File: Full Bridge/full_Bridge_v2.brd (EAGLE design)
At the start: 118.4 x 84.4 mm, 28 parts, among them Q1 IRF520, Q4 IRF520, Q5 IRF520, Q8 IRF520

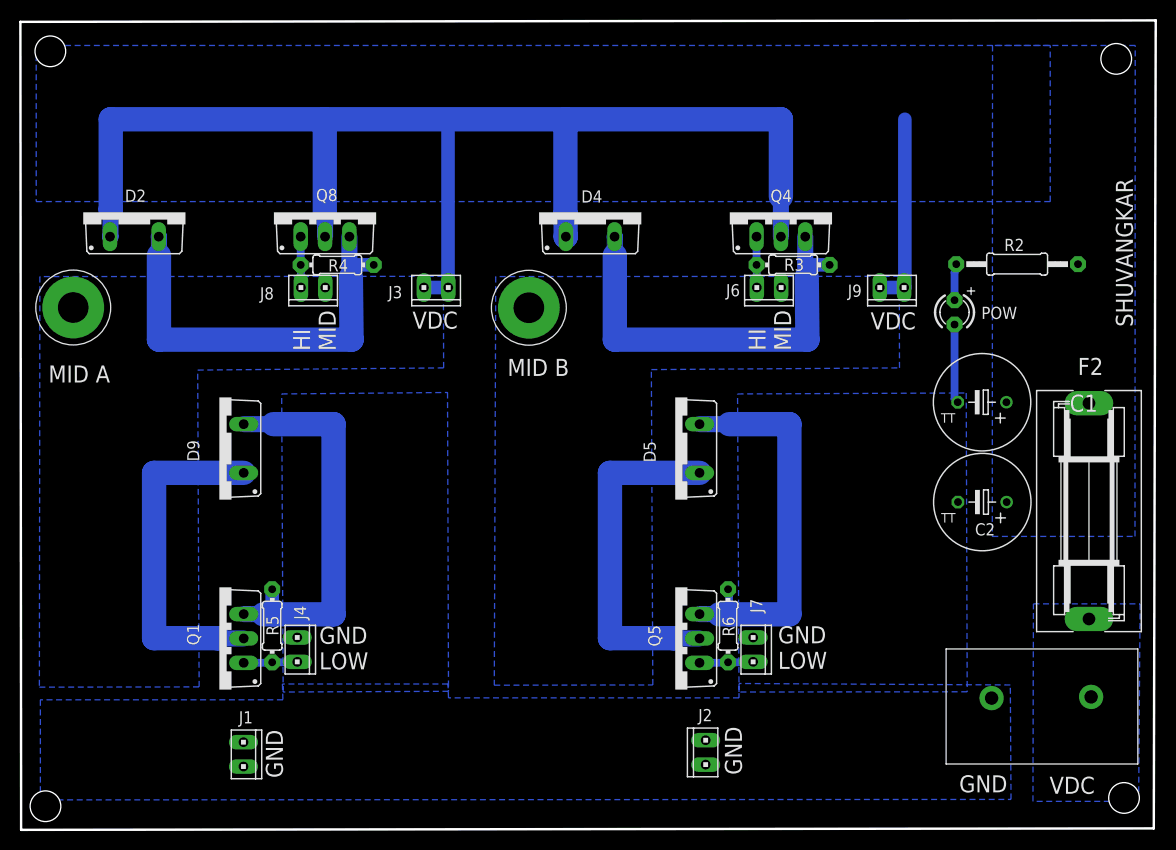
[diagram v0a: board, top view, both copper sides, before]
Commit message: h-bridge components value updated
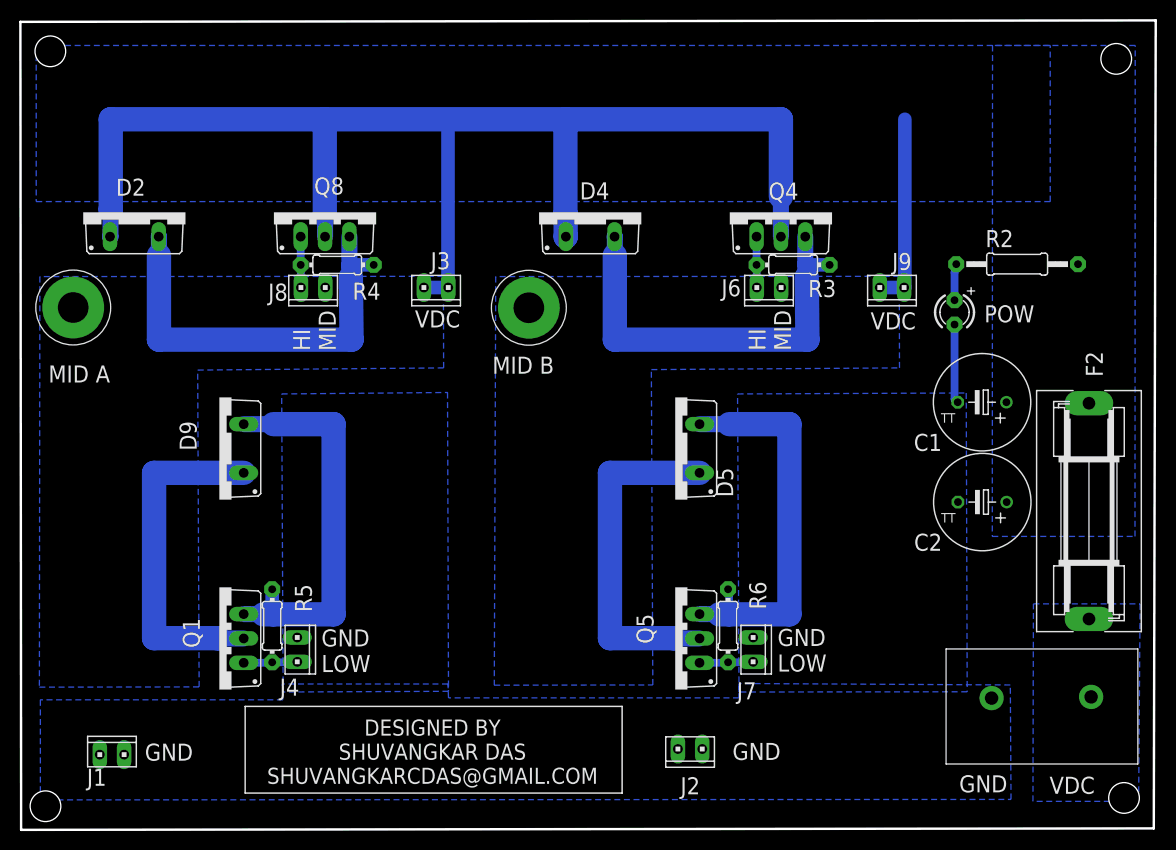
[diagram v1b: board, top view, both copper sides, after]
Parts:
- F2: value (none) -> 10A
- R2: value (none) -> 1k
- R3, R4, R5, R6: value (none) -> 10k
- moved J1 13.7 mm to (9.35, 6.58), turned to 0 degrees
- moved J2 1.66 mm to (69.6, 7.16), turned to 180 degrees
- renumbered U$3 to AC1, U$4 to AC2
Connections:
- net HVDC renamed DC_BUS
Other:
- board text added: "DESIGNED BY SHUVANGKAR DAS SHUVANGKARCDAS@GMAIL.COM"
- board text removed: "SHUVANGKAR"
